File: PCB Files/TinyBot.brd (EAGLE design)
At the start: 160 x 100 mm, 11 parts

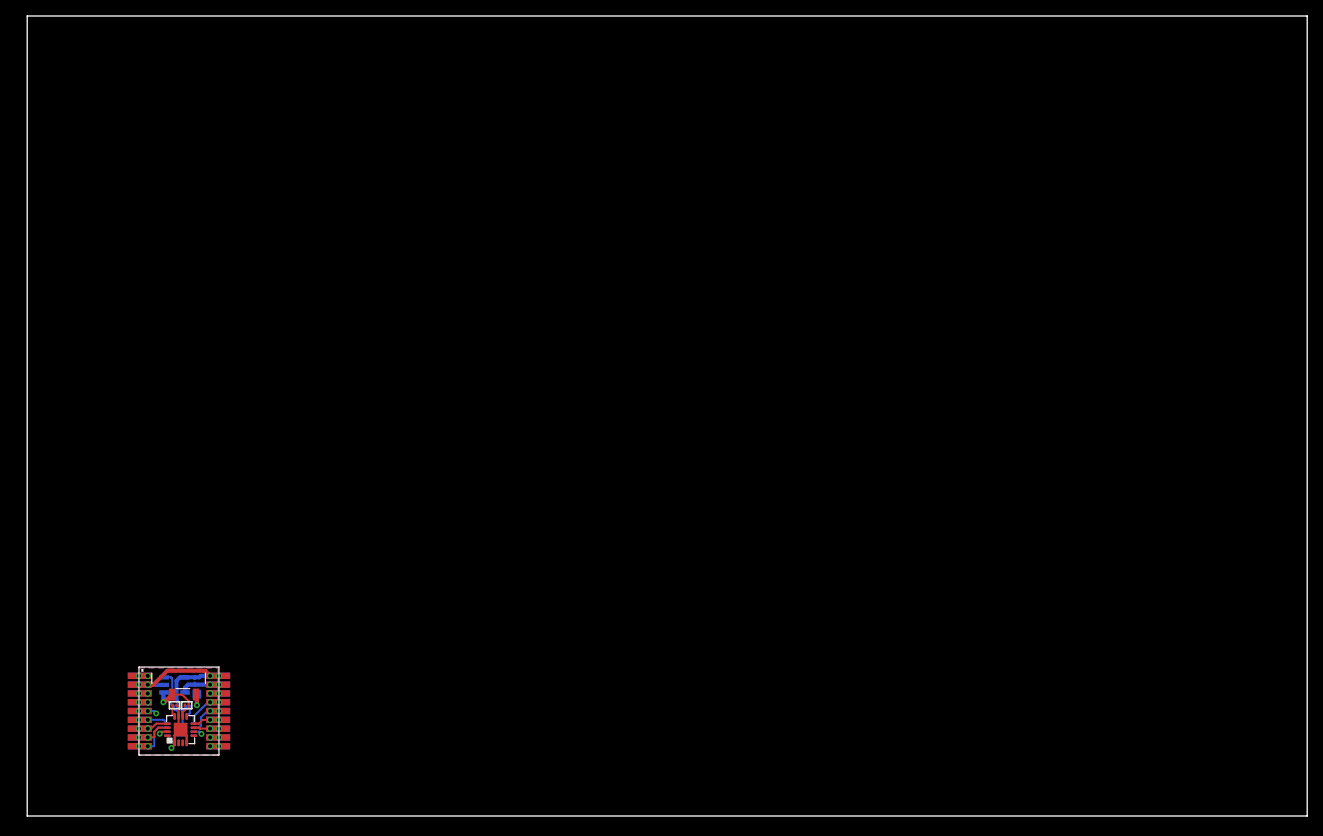
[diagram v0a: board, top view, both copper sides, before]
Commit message: PCB panel created and sent to PCBWay for review
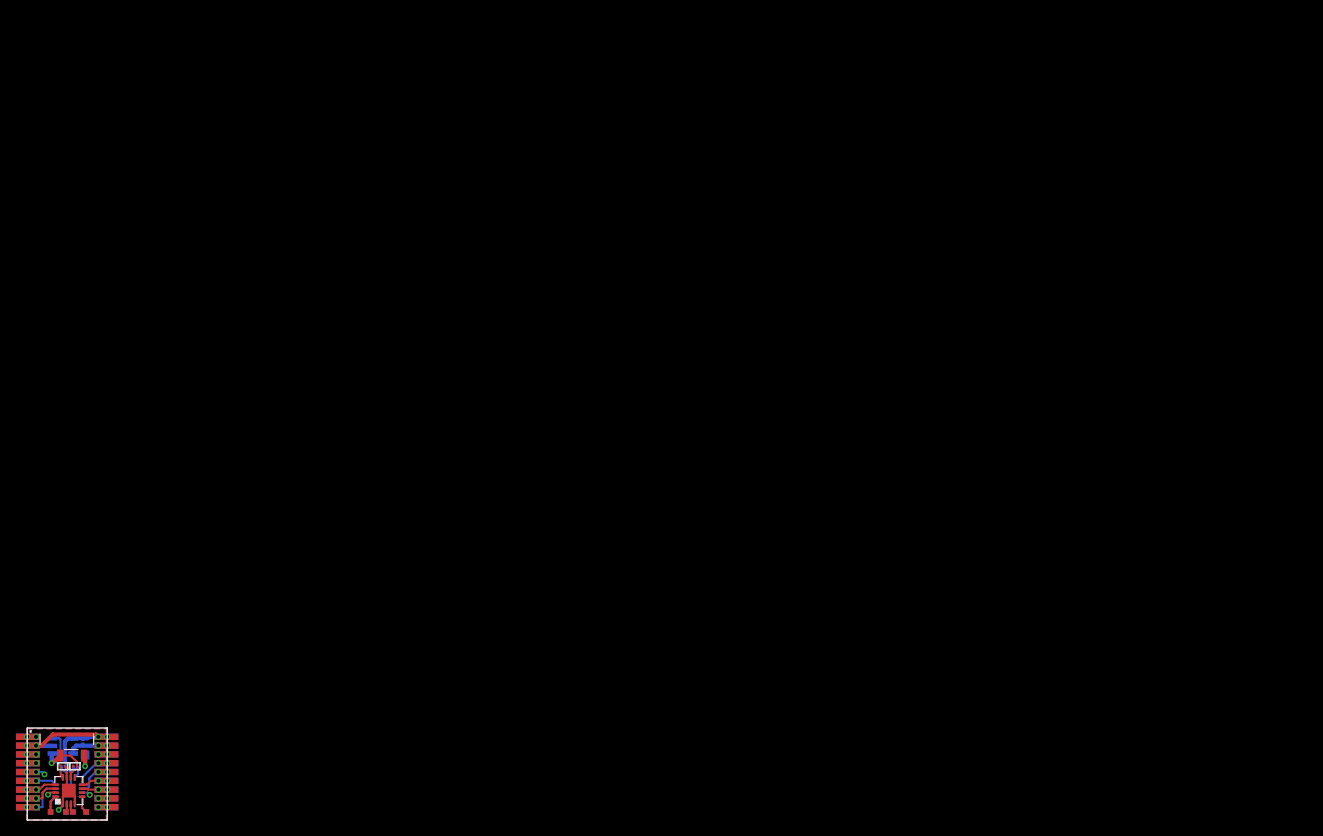
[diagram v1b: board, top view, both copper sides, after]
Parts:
- added TP1, TP2, TP3, TP4, TP5, TP6, TP7, TP8: TPTP07SQ, testpad:TP07SQ
- moved C2 15.9 mm to (4.57, 6.10)
- moved U$1 15.9 mm to (0.00, 0.00)
- moved C1 15.9 mm to (5.97, 6.22)
- moved C3 15.9 mm to (6.10, 6.10)
- moved C4 15.9 mm to (4.45, 6.22)
- moved C5 15.9 mm to (6.99, 9.27)
- moved LIPO_IN 15.9 mm to (7.24, 7.62)
- moved U$11 15.9 mm to (5.21, 3.17)
- moved U$16 15.9 mm to (5.21, 3.17)
- moved U$4 15.9 mm to (4.95, 9.65)
- moved U$5 15.9 mm to (4.45, 8.76)
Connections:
- new net AOUT1_A: TP1.TP, U$11.16
- new net AOUT1_B: TP5.TP, U$16.16
- new net AOUT2_A: TP2.TP, U$11.2
- new net AOUT2_B: TP6.TP, U$16.2
- new net BOUT1_A: TP3.TP, U$11.5
- new net BOUT1_B: TP7.TP, U$16.5
- new net BOUT2_A: TP4.TP, U$11.3
- new net BOUT2_B: TP8.TP, U$16.3
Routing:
- net BOUT1_B: track 0.00 -> 2.18 mm
- net AOUT1_A: track 0.00 -> 2.18 mm
- net BOUT1_A: track 0.00 -> 2.13 mm
- net AOUT1_B: track 0.00 -> 2.13 mm
- net BIN2_A: track 2.23 -> 4.33 mm
- net 3V3: track 4.13 -> 6.23 mm
- net BIN1_B: track 4.46 -> 6.46 mm
- net BIN2_B: track 2.65 -> 4.65 mm
- net AIN1_B: track 3.59 -> 5.59 mm
- net AIN2_A: track 2.81 -> 4.81 mm
- net BIN1_A: track 2.09 -> 4.09 mm
- net AIN2_B: track 3.68 -> 5.68 mm
- net BOUT2_A: track 0.00 -> 1.12 mm
- net AOUT2_B: track 0.00 -> 1.12 mm
- net BOUT2_B: track 0.00 -> 1.07 mm
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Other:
- board size 160 x 100 mm -> 10 x 11.5 mm

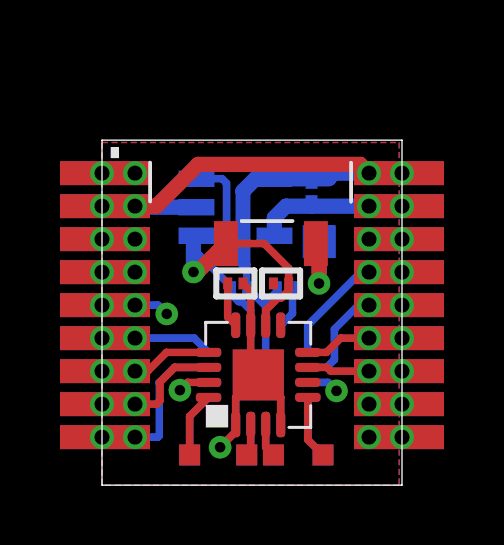
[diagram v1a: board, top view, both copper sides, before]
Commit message: PCB first order placed, cleared PCB panel files. ESP and Python Controller software written
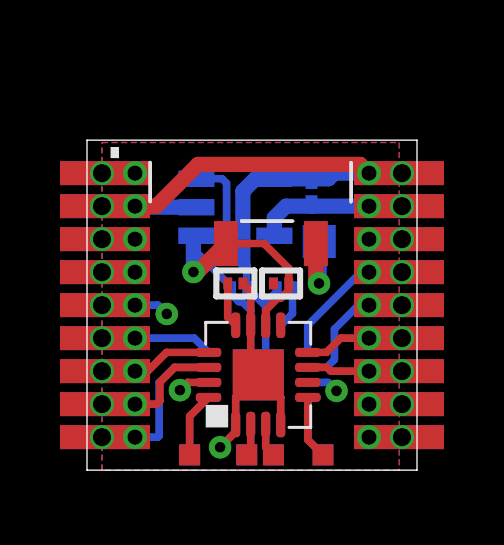
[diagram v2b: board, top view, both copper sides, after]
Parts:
- C1, C2: value (none) -> 4.7u
- C3, C4, C5: value (none) -> 2.2u
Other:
- board size 10 x 11.5 mm -> 11 x 11 mm
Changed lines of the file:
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@@
 <setting verticaltext="up"/>
 </settings>
-<grid distance="0.5" unitdist="mm" unit="mm" style="lines" multiple="1" display="yes" altdistance="0.5" altunitdist="mil" altunit="mil"/>
+<grid distance="0.5" unitdist="mm" unit="mm" style="lines" multiple="1" display="yes" altdistance="0.1" altunitdist="mm" altunit="mm"/>
 <layers>
 <layer number="1" name="Top" color="4" fill="1" visible="yes" active="yes"/>
@@
 <layer number="46" name="Milling" color="3" fill="1" visible="no" active="yes"/>
 <layer number="47" name="Measures" color="7" fill="1" visible="no" active="yes"/>
-<layer number="48" name="Document" color="7" fill="1" visible="yes" active="yes"/>
+<layer number="48" name="Document" color="7" fill="1" visible="no" active="yes"/>
 <layer number="49" name="Reference" color="7" fill="1" visible="no" active="yes"/>
 <layer number="50" name="dxf" color="7" fill="1" visible="no" active="no"/>
@@
 <board>
 <plain>
-<wire x1="0" y1="-0.5" x2="10" y2="-0.5" width="0" layer="20"/>
-<wire x1="10" y1="-0.5" x2="10" y2="11" width="0" layer="20"/>
-<wire x1="10" y1="11" x2="0" y2="11" width="0" layer="20"/>
-<wire x1="0" y1="11" x2="0" y2="-0.5" width="0" layer="20"/>
+<wire x1="-0.5" y1="0" x2="10.5" y2="0" width="0" layer="20"/>
+<wire x1="10.5" y1="0" x2="10.5" y2="11" width="0" layer="20"/>
+<wire x1="10.5" y1="11" x2="-0.5" y2="11" width="0" layer="20"/>
+<wire x1="-0.5" y1="11" x2="-0.5" y2="0" width="0" layer="20"/>
 </plain>
 <attributes>
@@
 <param name="mdViaViaSameLayer" value="6mil"/>
 <param name="mnLayersViaInSmd" value="2"/>
-<param name="mdCopperDimension" value="20mil"/>
+<param name="mdCopperDimension" value="0mil"/>
 <param name="mdDrill" value="6mil"/>
 <param name="mdSmdStop" value="0mil"/>
@@
 <param name="msMicroVia" value="9.99mm"/>
 <param name="msBlindViaRatio" value="0.5"/>
-<param name="rvPadTop" value="0.25"/>
-<param name="rvPadInner" value="0.25"/>
-<param name="rvPadBottom" value="0.25"/>
+<param name="rvPadTop" value="0.1"/>
+<param name="rvPadInner" value="0.1"/>
+<param name="rvPadBottom" value="0.1"/>
 <param name="rvViaOuter" value="0.25"/>
 <param name="rvViaInner" value="0.25"/>
@@
 <element name="U$1" library="esp8266modules" package="ESP01F" value="ESP01F" x="0" y="0" smashed="yes"/>
 <element name="U$5" library="SparkFun-IC-Power" package="SOT23-5" value="TLV755P" x="4.445" y="8.763" smashed="yes" rot="MR90"/>
-<element name="C1" library="rc-master-smd" package="C0201" value="" x="5.969" y="6.223" smashed="yes" rot="R180">
+<element name="C1" library="rc-master-smd" package="C0201" value="4.7u" x="5.969" y="6.223" smashed="yes" rot="R180">
 <attribute name="VALUE" x="6.731" y="7.493" size="0.6096" layer="27" ratio="10" rot="R180"/>
 </element>
-<element name="C4" library="rc-master-smd" package="C0201" value="" x="4.445" y="6.223" smashed="yes">
+<element name="C4" library="rc-master-smd" package="C0201" value="2.2u" x="4.445" y="6.223" smashed="yes">
 <attribute name="VALUE" x="3.683" y="4.953" size="0.6096" layer="27" ratio="10"/>
 </element>
 <element name="U$11" library="qfn16" package="QFN16" value="DRV8833C" x="5.207" y="3.175" smashed="yes" rot="R90"/>
-<element name="C2" library="rc-master-smd" package="C0201" value="" x="4.572" y="6.096" smashed="yes" rot="MR180">
+<element name="C2" library="rc-master-smd" package="C0201" value="4.7u" x="4.572" y="6.096" smashed="yes" rot="MR180">
 <attribute name="VALUE" x="3.81" y="7.366" size="0.6096" layer="28" ratio="10" rot="MR180"/>
 </element>
-<element name="C3" library="rc-master-smd" package="C0201" value="" x="6.096" y="6.096" smashed="yes" rot="MR0">
+<element name="C3" library="rc-master-smd" package="C0201" value="2.2u" x="6.096" y="6.096" smashed="yes" rot="MR0">
 <attribute name="VALUE" x="6.858" y="4.826" size="0.6096" layer="28" ratio="10" rot="MR0"/>
 </element>
@@
 <attribute name="VALUE" x="7.747" y="6.985" size="0.0254" layer="28" rot="MR0"/>
 </element>
-<element name="C5" library="rc-master-smd" package="C0201" value="" x="6.985" y="9.271" smashed="yes" rot="MR90">
+<element name="C5" library="rc-master-smd" package="C0201" value="2.2u" x="6.985" y="9.271" smashed="yes" rot="MR90">
 <attribute name="VALUE" x="5.715" y="8.509" size="0.6096" layer="28" ratio="10" rot="MR90"/>
 </element>
@@
 <vertex x="0" y="10.922"/>
 <vertex x="9.906" y="10.922"/>
-<vertex x="9.906" y="-0.5"/>
-<vertex x="0" y="-0.5"/>
+<vertex x="9.906" y="0"/>
+<vertex x="0" y="0"/>
 </polygon>
 <polygon width="0.1524" layer="1" isolate="0.1524" thermals="no">
 <vertex x="0" y="10.922"/>
 <vertex x="9.906" y="10.922"/>
-<vertex x="9.906" y="-0.5"/>
-<vertex x="0" y="-0.5"/>
+<vertex x="9.906" y="0"/>
+<vertex x="0" y="0"/>
 </polygon>
-<wire x1="9.9" y1="9.9" x2="10" y2="9.9" width="0" layer="19" extent="16-16"/>
-<wire x1="0" y1="8.8" x2="0.1" y2="8.8" width="0" layer="19" extent="1-1"/>
 </signal>
 <signal name="VINT_A">
@@
 <wire x1="6.985" y1="9.017" x2="6.985" y2="8.8" width="0.254" layer="16"/>
 <wire x1="9.9" y1="8.8" x2="8.9" y2="8.8" width="0.1524" layer="1"/>
-<wire x1="9.9" y1="8.8" x2="10" y2="8.8" width="0.1524" layer="16"/>
 <wire x1="9.9" y1="8.8" x2="8.9" y2="8.8" width="0.1524" layer="16"/>
+<wire x1="9.9" y1="8.8" x2="10" y2="8.8" width="0" layer="19" extent="16-16"/>
 </signal>
 <signal name="AIN1_B">
@@
 <wire x1="7.747" y1="4.699" x2="8.548" y2="5.5" width="0.254" layer="16"/>
 <wire x1="8.548" y1="5.5" x2="8.9" y2="5.5" width="0.254" layer="16"/>
-<wire x1="9.9" y1="5.5" x2="10" y2="5.5" width="0.254" layer="16"/>
 <wire x1="9.9" y1="5.5" x2="8.9" y2="5.5" width="0.1524" layer="1"/>
 <wire x1="9.9" y1="5.5" x2="8.9" y2="5.5" width="0.1524" layer="16"/>
+<wire x1="9.9" y1="5.5" x2="10" y2="5.5" width="0" layer="19" extent="16-16"/>
 </signal>
 <signal name="AIN2_B">
@@
 <wire x1="1.522" y1="3.3" x2="1.1" y2="3.3" width="0.254" layer="1"/>
 <wire x1="2.147" y1="3.925" x2="1.522" y2="3.3" width="0.254" layer="1"/>
-<wire x1="0.1" y1="3.3" x2="0" y2="3.3" width="0.254" layer="1"/>
 <wire x1="0.1" y1="3.3" x2="1.1" y2="3.3" width="0.1524" layer="16"/>
 <wire x1="0.1" y1="3.3" x2="1.1" y2="3.3" width="0.1524" layer="1"/>
+<wire x1="0.1" y1="3.3" x2="0" y2="3.3" width="0" layer="19" extent="1-1"/>
 </signal>
 <signal name="BIN1_A">
@@
 <wire x1="7.481" y1="3.925" x2="7.956" y2="4.4" width="0.254" layer="1"/>
 <wire x1="9.9" y1="4.4" x2="8.9" y2="4.4" width="0.1524" layer="16"/>
-<wire x1="9.9" y1="4.4" x2="10" y2="4.4" width="0.1524" layer="1"/>
 <wire x1="9.9" y1="4.4" x2="8.9" y2="4.4" width="0.1524" layer="1"/>
+<wire x1="9.9" y1="4.4" x2="10" y2="4.4" width="0" layer="19" extent="1-1"/>
 </signal>
 <signal name="V_BAT">
@@
 <signal name="LIPO_IN">
 <contactref element="U$4" pad="L2"/>
-<wire x1="7.2344" y1="7.4476" x2="7.2344" y2="6.223" width="0.508" layer="1"/>
 <via x="7.2344" y="6.223" extent="1-16" drill="0.35"/>
 <contactref element="LIPO_IN" pad="TP"/>
-<wire x1="7.239" y1="7.62" x2="7.2344" y2="7.6154" width="0.508" layer="16"/>
-<wire x1="7.2344" y1="7.6154" x2="7.2344" y2="6.223" width="0.508" layer="16"/>
-<wire x1="7.2344" y1="7.6154" x2="7.13" y2="7.552" width="0" layer="19" extent="1-16"/>
+<wire x1="7.13" y1="7.552" x2="7.13" y2="6.3274" width="0.508" layer="1"/>
+<wire x1="7.13" y1="6.3274" x2="7.2344" y2="6.223" width="0.508" layer="1"/>
+<wire x1="7.2344" y1="6.223" x2="7.2344" y2="7.6154" width="0.508" layer="16"/>
+<wire x1="7.2344" y1="7.6154" x2="7.239" y2="7.62" width="0.508" layer="16"/>
 </signal>
 <signal name="AOUT1_A">
